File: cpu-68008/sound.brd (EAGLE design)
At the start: 99.7 x 99.7 mm, 59 parts, among them IC101 GAL22V10D, IC102 74HCT175N, IC201 YM3812, IC202 YM3014B, IC203 AY-3-8910, IC301 TL062, IC302 TL062, IC401 74HCT14N, IC402 TL16C550D, J401 DIN5, J402 DIN5

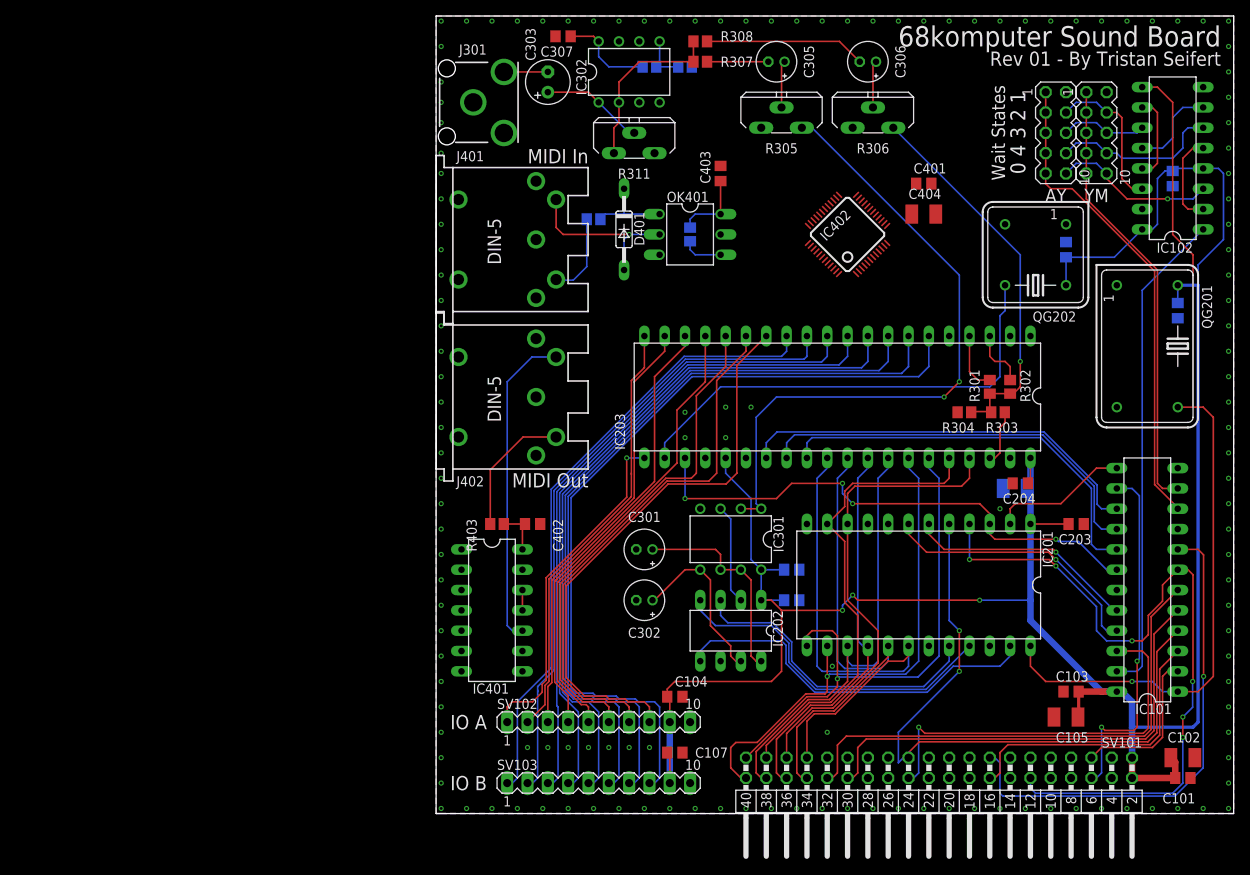
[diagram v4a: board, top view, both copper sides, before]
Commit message: finished routing sound board; added correct CPU board PLDs
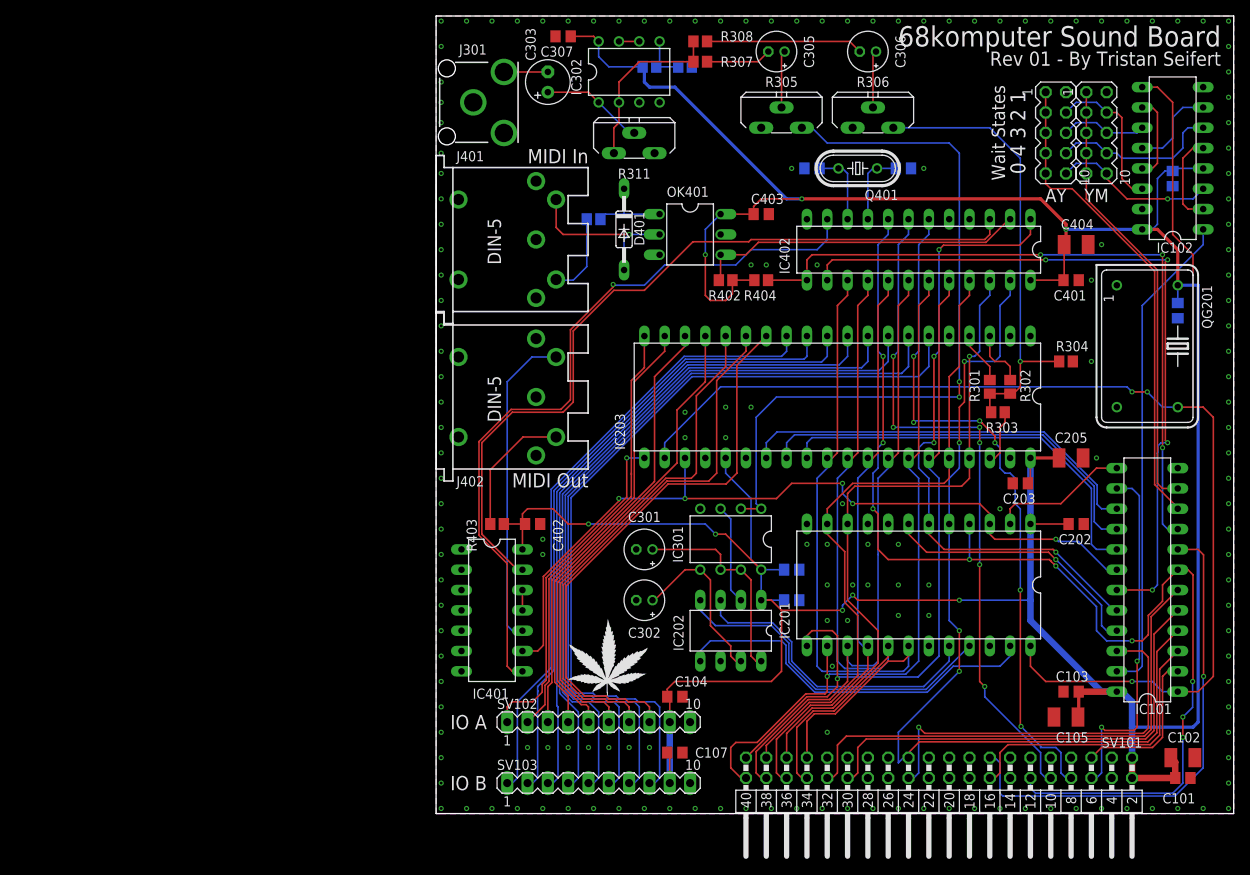
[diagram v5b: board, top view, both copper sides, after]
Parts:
- removed C206: 10µF, rcl:SMC_B
- removed QG202: (no value), crystal:DIL08S
- added C405, C406: 27pF, rcl:C0805
- added Q401: 3MHz, crystal:HC49/S
- added R404: 4k7, rcl:R2012
- added WEED401: WEED, 68komputer:DOINK
- C205: value 100nF -> 10µF; device rcl:C0805 -> rcl:SMC_B
- IC402: value TL16C550D -> SCC2691; device 68komputer:LQFP48 -> 68komputer:DIL24S
- moved C205 39.2 mm to (79.4, 44.5), flipped to the top, turned to 0 degrees
- moved C202 34.3 mm to (80.0, 36.2), flipped to the top, turned to 0 degrees
- moved C204 32.1 mm to (44.5, 26.7), flipped to the bottom
- moved C401 22.0 mm to (79.4, 66.7)
- moved C404 19.4 mm to (80.0, 71.1)
- moved R304 14.2 mm to (78.7, 56.5), turned to 180 degrees
- moved IC402 9.09 mm to (60.3, 70.5), turned to 180 degrees
- moved C203 8.64 mm to (73.0, 41.3), turned to 180 degrees
- moved R402 7.24 mm to (36.2, 66.7), flipped to the top, turned to 0 degrees
- moved C403 7.18 mm to (40.6, 74.9), turned to 0 degrees
- moved C305 1.27 mm to (42.5, 95.2)
- moved C306 1.27 mm to (54.0, 95.2)
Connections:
- removed net CLK_B: IC203.22, IC402.14, QG202.5
- removed net MIDI_IRQ: IC101.9, IC402.30
- removed net N$3: IC402.12, IC402.5
- removed net N$8: IC402.10, IC402.9
- removed net VCC: IC402.42
- new net !MIDI_IRQ: IC101.9, IC402.13, R404.1
- new net MIDI_UART_X1: C405.2, IC402.9, Q401.1
- new net MIDI_UART_X2: C406.2, IC402.10, Q401.2
- net !MIDI_UART_CS: now also IC402.14; no longer IC402.11
- net !RD: now also IC402.1; no longer IC402.19
- net !SLOT_AS: no longer IC402.24
- net +5V: now also C205.+, IC402.24, R404.2; no longer C205.1, C206.+, QG202.8
- net CLK_A: now also IC203.22
- net GND: now also C205.-, C405.1, C406.1, IC402.12; no longer C205.2, C206.-, IC402.18, QG202.4
- net MIDI_RESET: now also IC402.11; no longer IC402.35
- net MIDI_RX: now also IC402.2; no longer IC402.7
- net MIDI_TX: now also IC402.3; no longer IC402.8
- net SLOT_A0: now also IC402.8; no longer IC402.28
- net SLOT_A1: now also IC402.7; no longer IC402.27
- net SLOT_A2: now also IC402.6; no longer IC402.26
- net SLOT_D0: now also IC402.22; no longer IC402.43
- net SLOT_D1: now also IC402.21; no longer IC402.44
- net SLOT_D2: now also IC402.20; no longer IC402.45
- net SLOT_D3: now also IC402.19; no longer IC402.46
- net SLOT_D4: now also IC402.18; no longer IC402.47
- net SLOT_D5: now also IC402.17; no longer IC402.2
- net SLOT_D6: now also IC402.16; no longer IC402.3
- net SLOT_D7: now also IC402.15; no longer IC402.4
- net SLOT_R/!W!: now also IC402.23; no longer IC402.16
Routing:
- net +5V: track 313.1 -> 432.1 mm, vias 3 -> 8
- net MIDI_TX: track 0.00 -> 99.7 mm
- net MIDI_RESET: track 0.00 -> 93.6 mm, vias 0 -> 1
- net !MIDI_UART_CS: track 0.00 -> 91.9 mm, vias 0 -> 4
- net !MIDI_IRQ: track 0.00 -> 87.9 mm, vias 0 -> 3
- net SLOT_A2: track 0.00 -> 85.8 mm, vias 0 -> 6
- net SLOT_A1: track 0.00 -> 85.5 mm, vias 0 -> 6
- net CLK_A: track 108.6 -> 178.6 mm, vias 1 -> 3
- net CLK_B: track 58.9 -> 0.00 mm
- net SLOT_A0: track 92.6 -> 147.4 mm, vias 6 -> 9
- net !RD: track 28.7 -> 79.4 mm, vias 1 -> 4
- net MIDI_RX: track 5.13 -> 41.3 mm
- net SLOT_R/!W!: track 81.6 -> 117.5 mm, vias 2 -> 4
- net !RESET: track 66.5 -> 100.0 mm, vias 4 -> 5
- net SLOT_D0: track 59.4 -> 83.1 mm, vias 0 -> 1
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
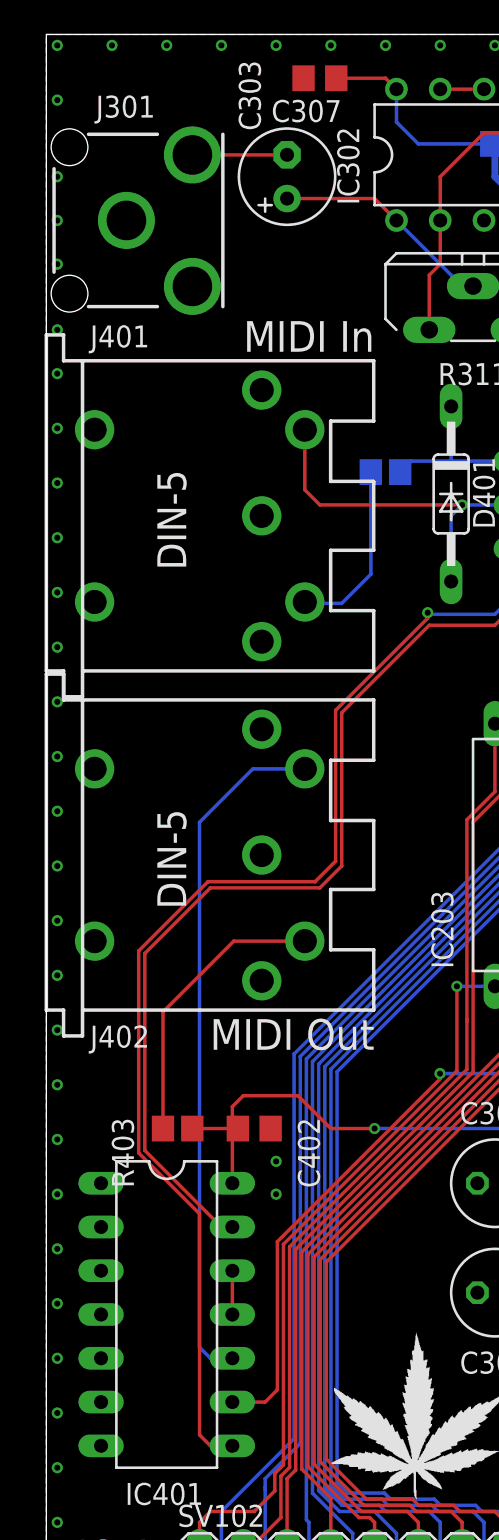
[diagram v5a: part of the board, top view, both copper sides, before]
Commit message: Added 8-bit IDE board Finished routing of sound board
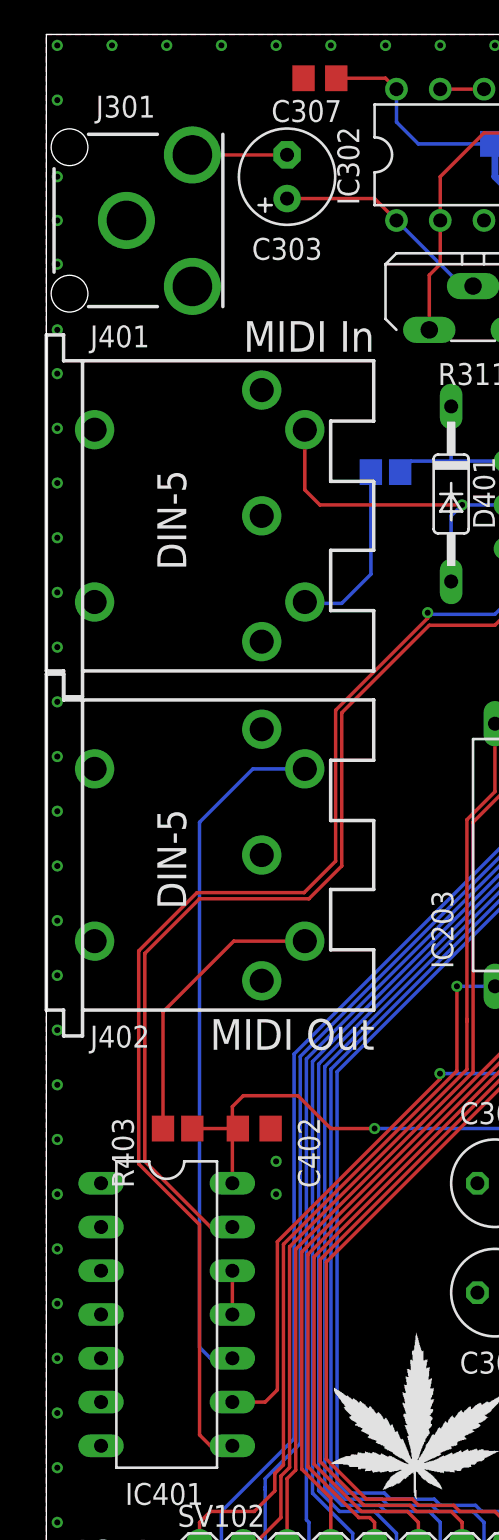
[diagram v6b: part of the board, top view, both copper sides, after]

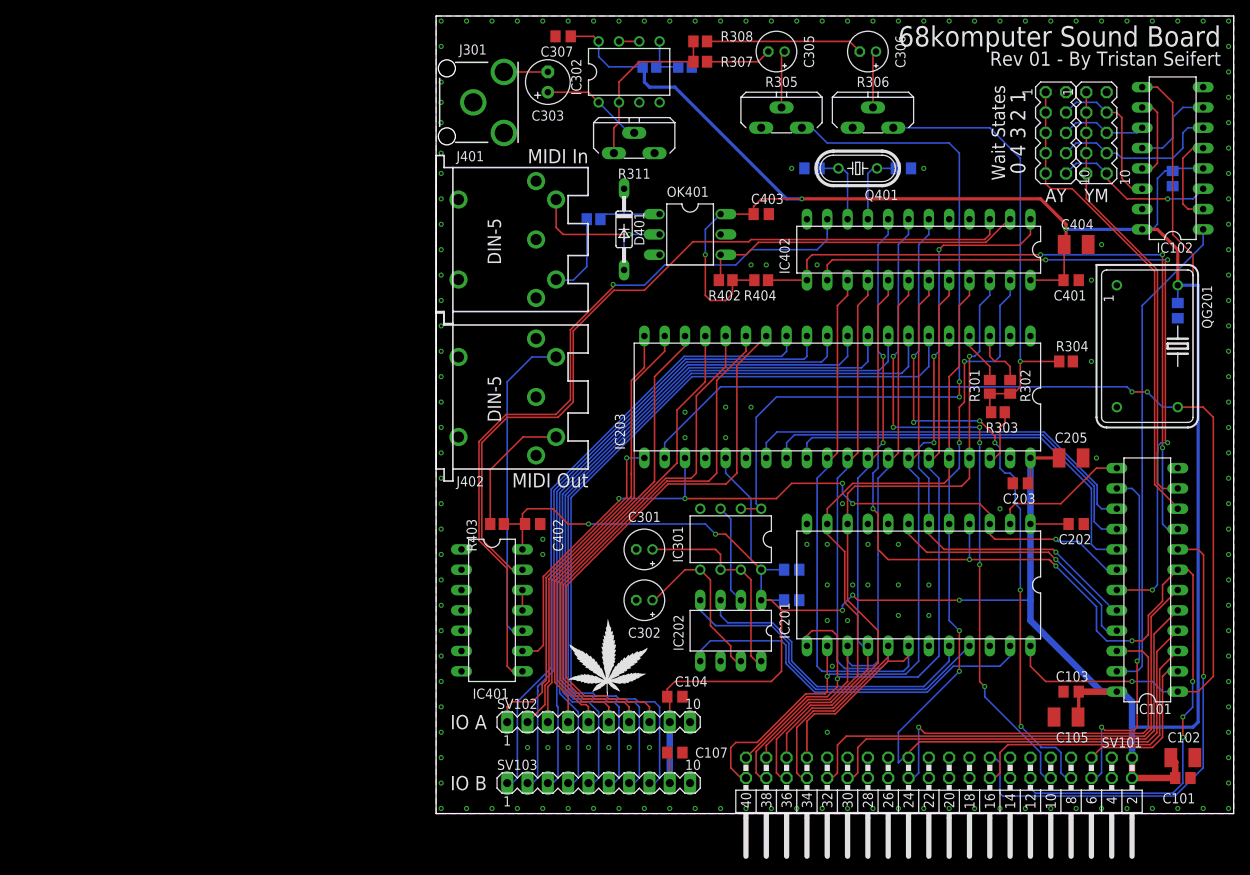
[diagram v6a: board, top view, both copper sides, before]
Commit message: added /DS to GALs on all peripherals and backplane began work on TMS9918 video card
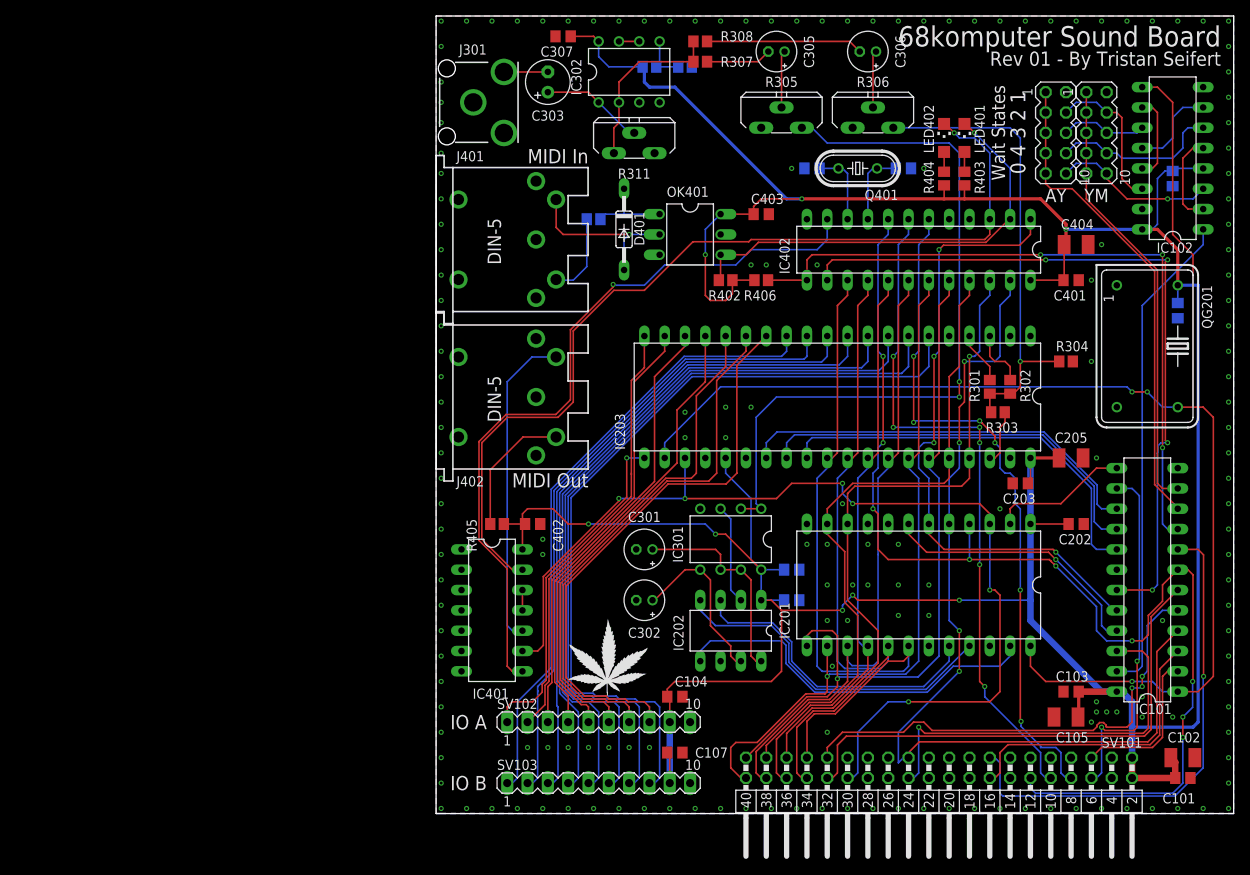
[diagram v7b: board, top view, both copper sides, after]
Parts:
- added LED401, LED402: (no value), led:CHIPLED_1206
- added R405: 220R, rcl:R2012
- added R406: 4k7, rcl:R2012
- R403: value 220R -> 3k
- R404: value 4k7 -> 3k
- moved R403 72.6 mm to (66.0, 79.4), turned to 90 degrees
- moved R404 26.2 mm to (63.5, 79.4), turned to 90 degrees
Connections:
- removed net !RESET: IC101.18, IC201.3, IC203.23, IC401.9
- new net N$3: LED401.A, R403.2
- new net N$8: LED402.A, R404.2
- net !MIDI_IRQ: now also R406.1; no longer R404.1
- net !SLOT_DS: now also IC101.5
- net !SLOT_RESET: now also IC201.3, IC203.23, IC401.9; no longer IC101.5
- net +5V: now also R403.1, R404.1, R405.2, R406.2; no longer R403.2, R404.2
- net MIDI_RX: now also LED401.C
- net MIDI_TX: now also LED402.C
- net N$17: now also R405.1; no longer R403.1
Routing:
- net !RESET: track 100.0 -> 0.00 mm, vias 5 -> 0
- net !SLOT_RESET: track 58.9 -> 129.4 mm, vias 0 -> 6
- net !SLOT_DS: track 0.00 -> 60.3 mm, vias 0 -> 3
- net MIDI_TX: track 100.1 -> 115.6 mm, vias 0 -> 1
- net MIDI_RX: track 41.3 -> 55.7 mm, vias 0 -> 1
- net +5V: track 432.1 -> 435.5 mm
- net N$8: track 0.00 -> 2.48 mm
- net N$3: track 0.00 -> 2.48 mm
- net PSG_OUT: track 57.4 -> 58.9 mm
